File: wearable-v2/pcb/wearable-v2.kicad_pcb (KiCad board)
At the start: 2 copper layers, 78 parts, among them U10 ATmega328PB-M, U11 TMP1075, U12 MAX30102, U13 TCR3UFxxA, U14 LIS2DE12, U2 MCP73832-2-OT, U4 FT201XQ, U9 APDS-9250, Y1 32.768kHz

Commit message: Additional V2 wearable design work
Signed-off-by: Adam Fowler <adam@adamfowler.org>
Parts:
- moved TP16 154.2 mm to (273.6, 19.6)
- moved TP12 148.0 mm to (264.1, 19.8)
- moved TP13 148.0 mm to (264.1, 22.8)
- moved TP14 148.0 mm to (264.1, 25.9)
- moved TP15 148.0 mm to (264.1, 28.9)
- moved U14 142.0 mm to (222.8, 37.1)
- moved C24 121.2 mm to (249.3, 42.1)
- moved C25 120.5 mm to (251.2, 57.4)
- moved C26 120.5 mm to (251.2, 59.4)
- moved TP18 109.5 mm to (229.1, 34.8)
- moved TP17 103.6 mm to (226.8, 42.2)
- moved C21 103.0 mm to (36.4, 24.1)
- moved C17 98.5 mm to (29.6, 29.4)
- moved C18 97.0 mm to (34.3, 28.4)
- moved C28 96.7 mm to (222.3, 46.0)
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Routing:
- net +BATT: track 0.00 -> 25.4 mm
- net /Standard Connector/BT_STAT: track 0.00 -> 23.2 mm
- net GND: track 0.00 -> 21.5 mm, vias 0 -> 5
- net /Bio Board V1/SDA: track 0.00 -> 20.6 mm, vias 0 -> 2
- net /Bio Board V1/SCL: track 0.00 -> 19.7 mm
- net VDD: track 0.00 -> 15.0 mm, vias 0 -> 3
- net VBUS: track 0.00 -> 6.62 mm
- net /Standard Connector/CH_STAT: track 0.00 -> 6.15 mm
- net /Light Sensor Panel V1/LS_INT: track 0.00 -> 4.48 mm
- net Net-(U4-3V3OUT): track 0.00 -> 3.85 mm
- net /Standard Connector/USB_D-: track 0.00 -> 1.99 mm
- net /Standard Connector/USB_D+: track 0.00 -> 1.69 mm
- net Net-(D1-A): track 0.00 -> 1.61 mm
- net Net-(U4-USBDP): track 0.00 -> 1.54 mm
- net Net-(U4-USBDM): track 0.00 -> 1.54 mm
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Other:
- board text added: "ANT"
- board text added: "Bio Board Here"
- board text added: "Compute Board Here"
- board text added: "Deleted???"
- board text added: "Display Board Here"
- board text added: "Front Button Panel"
- board text added: "Front Light Sensor Panel"
- board text added: "GNSS"
- board text added: "Positioning Board Here"
- board text added: "USB-C Here"

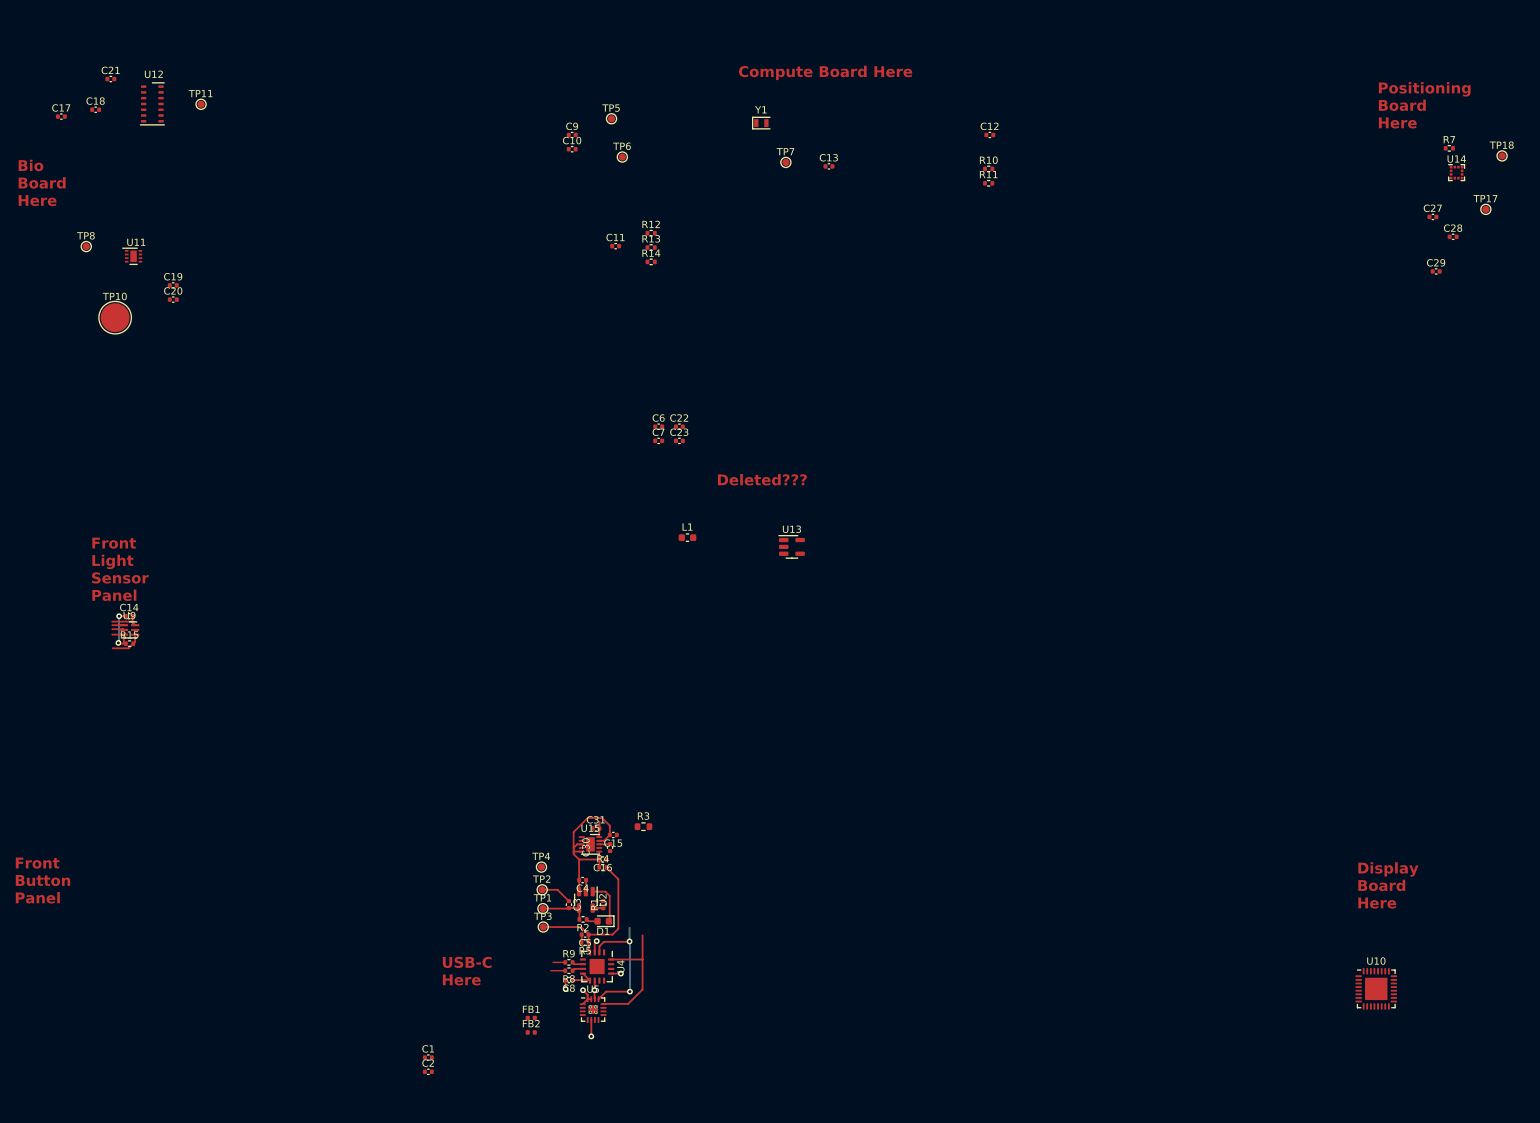
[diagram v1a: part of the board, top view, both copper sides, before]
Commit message: Updated components and PCB layout
Signed-off-by: Adam Fowler <adam@adamfowler.org>
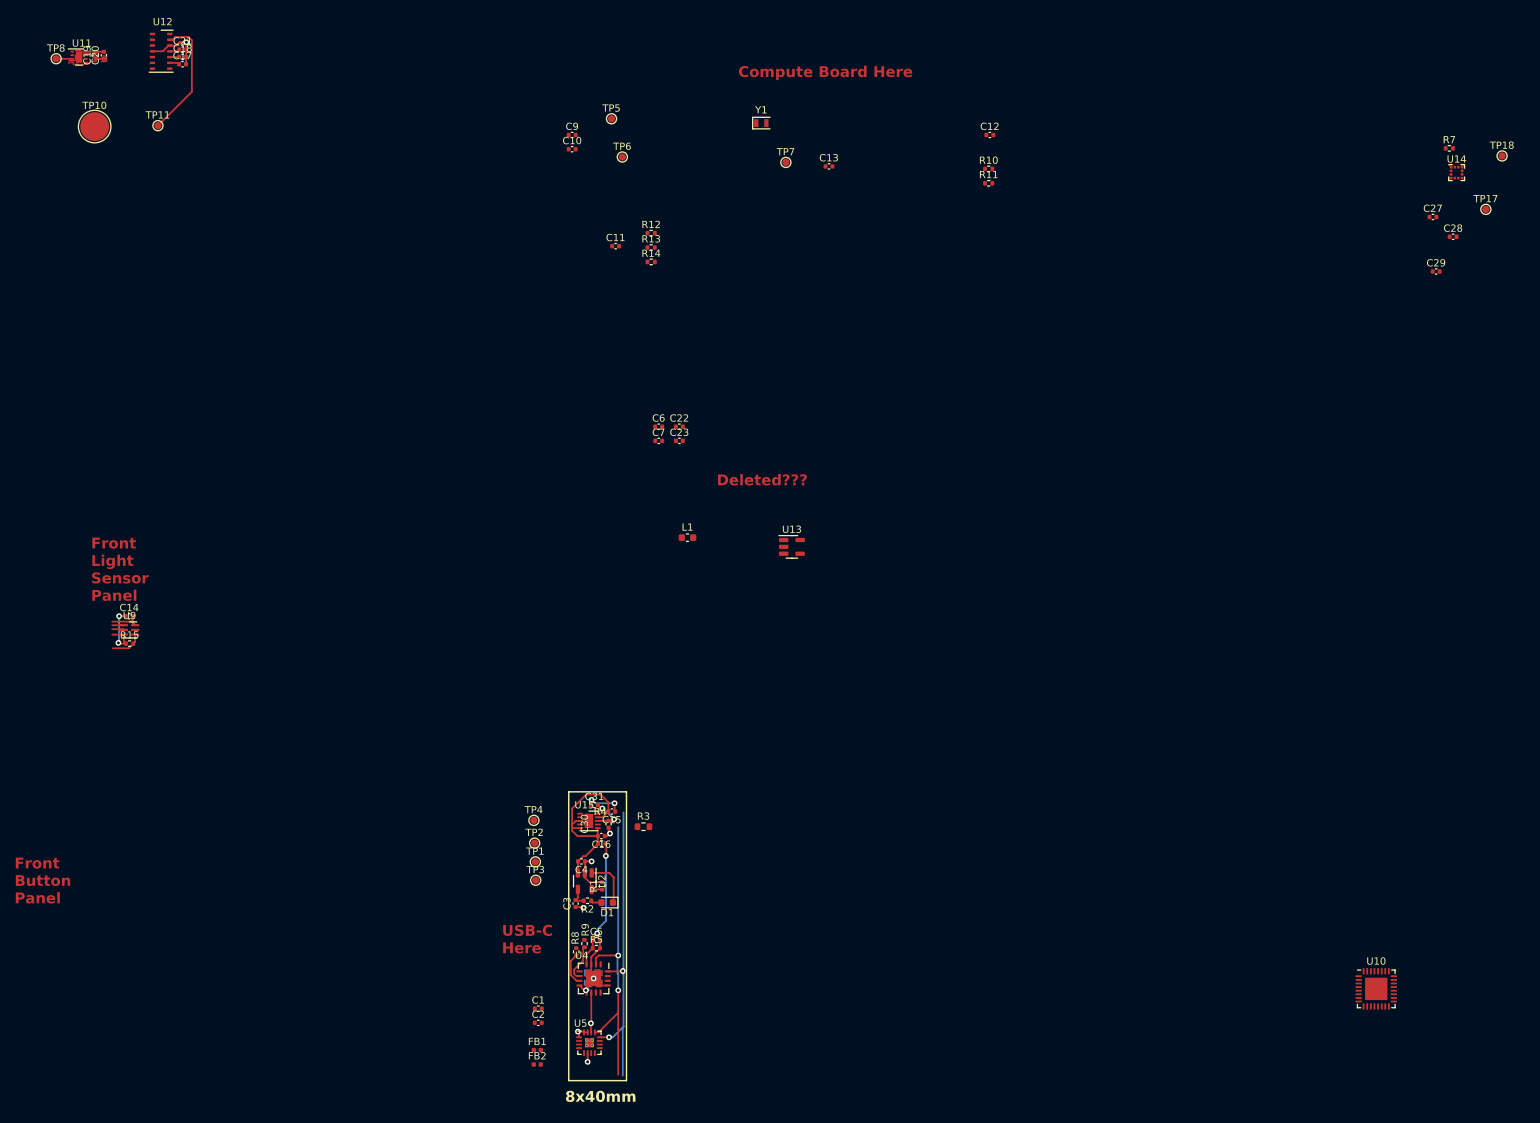
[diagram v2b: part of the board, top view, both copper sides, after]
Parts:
- C8: moved to B.Cu
- moved C20 35.2 mm to (35.4, 20.9), turned to 90 degrees
- moved C19 33.6 mm to (34.3, 20.9), turned to 90 degrees
- moved U11 28.6 mm to (32.0, 21.1)
- moved TP10 26.6 mm to (34.2, 30.7)
- moved TP8 26.3 mm to (28.8, 21.3)
- moved C17 18.3 mm to (46.3, 22.1)
- moved C1 16.7 mm to (95.6, 152.9)
- moved C2 16.7 mm to (95.6, 154.9)
- moved C18 14.1 mm to (46.4, 21.1)
- moved C21 10.8 mm to (46.4, 20.1)
- moved U12 7.39 mm to (43.4, 20.3)
- moved TP11 6.67 mm to (42.9, 30.6)
- moved TP1 6.56 mm to (95.2, 132.6)
- moved TP3 6.56 mm to (95.2, 135.1)
- moved TP4 6.56 mm to (95.0, 126.8)
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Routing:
- net /Bio Board V1/SCL: track 19.7 -> 44.9 mm, vias 0 -> 2
- net /Bio Board V1/SDA: track 20.6 -> 44.8 mm
- net GND: track 21.5 -> 40.1 mm, vias 5 -> 9
- net /Bio Board V1/BIO_INT: track 0.00 -> 17.2 mm
- net VDD: track 15.0 -> 27.3 mm, vias 3 -> 5
- net /Standard Connector/BT_STAT: track 23.2 -> 18.0 mm, vias 0 -> 2
- net VBUS: track 6.62 -> 2.92 mm
- net Net-(U4-USBDP): track 1.54 -> 5.15 mm
- net Net-(U4-USBDM): track 1.54 -> 4.55 mm
- net /Bio Board V1/TMP_INT: track 0.00 -> 2.23 mm
- net /Standard Connector/USB_D-: track 1.99 -> 0.00 mm
- net Net-(U4-3V3OUT): track 3.85 -> 1.98 mm, vias 0 -> 1
- net /Standard Connector/USB_D+: track 1.69 -> 0.00 mm
- net +BATT: track 25.4 -> 26.3 mm
- net /Standard Connector/CH_STAT: track 6.15 -> 6.85 mm
- added copper zone on B.Cu, net GND
- added copper zone on F.Cu, net GND
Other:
- board text added: "35x19mm"
- board text added: "46x46mm"
- board text added: "8x40mm"

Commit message: Further V2 routing
Signed-off-by: Adam Fowler <adam@adamfowler.org>
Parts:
- added ANT1: ~, Herald:NN02-224, F.Cu at (242.1, 59.6)
- added BT1: LiPo, Herald:Herald_Battery_Solder_Pads, F.Cu at (104.8, 117.9)
- added D2: LED_ARBG, Herald:LED_Kingbright_APHF1608, F.Cu at (190.9, 34.3)
- added H1: ThermalSlot, Herald:MillSlot_8.0x1.0mm, F.Cu at (91.4, 81.4)
- added IC1: TESEO-LIV3F, Herald:SON110P970X1010X230-18N, F.Cu at (260.7, 71.7)
- added J7: USB_C_Receptacle_USB2.0, Herald:USB_C_Receptacle_IPxx, F.Cu at (101.1, 142.9)
- added SW1: SW_Push, Button_Switch_SMD:SW_Push_1P1T_NO_CK_KSC6xxJ, F.Cu at (100.6, 172.1)
- added U1: DT1446-04V, Herald:SOT-563, F.Cu at (107.2, 142.9)
- added U3: S-85S1A, Herald:SNT-6A, F.Cu at (114.6, 119.3)
- added U6: BC833, Herald:Fanstel_BC833x, F.Cu at (189.4, 25.6)
- added U7: MX25R8035FZxxx0, Herald:USON-8-1EP_2x3mm_P0.5mm_EP0.25x1.65mm, F.Cu at (184.7, 23.0)
- added U8: PCF85063ATL, Herald:DFN-10-1EP_2.6x2.6mm_P0.5mm_EP1.25x2.15mm, F.Cu at (185.2, 18.3)
- moved C9 86.0 mm to (186.3, 31.1), turned to -90 degrees
- moved R12 83.0 mm to (193.2, 32.3), turned to -90 degrees
- moved R13 82.2 mm to (192.0, 32.3), turned to -90 degrees
- moved R14 81.4 mm to (190.8, 32.3), turned to -90 degrees
- moved TP6 70.8 mm to (178.1, 34.2)
- moved TP5 69.9 mm to (175.5, 34.2)
- moved TP7 63.6 mm to (191.1, 18.5)
- moved Y1 63.1 mm to (188.6, 18.9), turned to 180 degrees
- moved C6 44.6 mm to (115.1, 116.8)
- moved L1 32.3 mm to (118.2, 119.9)
- moved R10 30.0 mm to (185.9, 25.8), turned to 180 degrees
- moved R11 29.2 mm to (182.2, 22.4)
- moved C12 27.2 mm to (182.2, 19.3)
- moved FB2 25.2 mm to (103.6, 136.8), turned to 180 degrees
- moved FB1 22.6 mm to (101.1, 136.8)
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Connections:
- C10 pad 1: VDD -> VDD1
- C11 pad 1: VDD -> VDD1
- C12 pad 2: VDD -> VDD1
- C13 pad 1: VDD -> VDD1
- C14 pad 1: VDD -> +1V8
- C17 pad 1: VDD -> +1V8
- C18 pad 1: VDD -> +1V8
- C19 pad 2: VDD -> +1V8
- C20 pad 2: VDD -> +1V8
- C21 pad 1: VDD -> +1V8
- C23 pad 1: VDD -> +1V8
- C24 pad 1: VDD -> VDD1
- C30 pad 2: VDD -> VDD1
- C31 pad 2: VDD -> +1V8
- R10 pad 1: VDD -> VDD1
- R11 pad 1: VDD -> VDD1
- R15 pad 1: VDD -> +1V8
- TP12 pad 1: VDD -> VDD1
- U10 pad 18: VDD -> VDD1
- U10 pad 4: VDD -> VDD1
- U11 pad 8: VDD -> +1V8
- U12 pad 10: VDD -> +1V8
- U12 pad 11: VDD -> +1V8
- U12 pad 9: VDD -> +1V8
- U13 pad 5: VDD -> +1V8
- U15 pad 10: VDD -> +1V8
- U15 pad 8: VDD -> VDD1
- U9 pad 3: VDD -> +1V8
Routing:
- net /Compute - Fanstel BC833M - Nordic Semi nRF52833 based/SWDCLK: track 0.00 -> 24.5 mm, vias 0 -> 2
- net /Compute - Fanstel BC833M - Nordic Semi nRF52833 based/SWDIO: track 0.00 -> 23.6 mm, vias 0 -> 2
- net VDD: track 27.3 -> 9.15 mm
- net Earth: track 0.00 -> 17.9 mm
- net GNDPWR: track 0.00 -> 15.7 mm
- net +1V8: track 0.00 -> 15.3 mm
- net /Bio Board V1/SDA: track 44.8 -> 58.9 mm
- net /Compute - Fanstel BC833M - Nordic Semi nRF52833 based/LED_B: track 0.00 -> 12.7 mm, vias 0 -> 2
- net VBUS: track 2.92 -> 12.0 mm
- net /Standard Connector/USB_D-: track 0.00 -> 8.76 mm, vias 0 -> 2
- net /Compute - Fanstel BC833M - Nordic Semi nRF52833 based/NFC2: track 0.00 -> 8.72 mm
- net /Compute - Fanstel BC833M - Nordic Semi nRF52833 based/RTC_INT: track 0.00 -> 8.04 mm
- net /Standard Connector/BT_STAT: track 18.0 -> 25.9 mm
- net /Compute - Fanstel BC833M - Nordic Semi nRF52833 based/NFC1: track 0.00 -> 7.51 mm
- net /Compute - Fanstel BC833M - Nordic Semi nRF52833 based/FLASH_CS: track 0.00 -> 7.45 mm
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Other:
- board text removed: "USB-C Here"

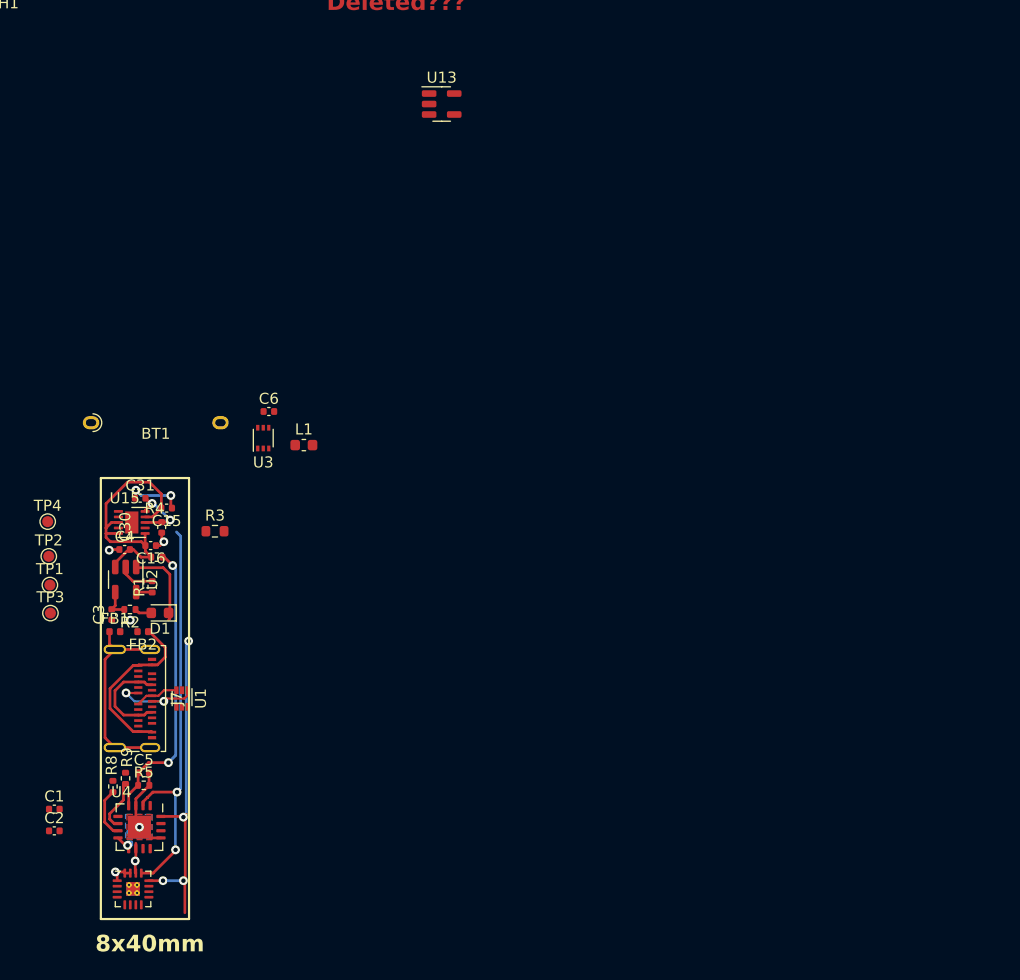
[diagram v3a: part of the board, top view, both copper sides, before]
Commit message: Replaced unavailable I2C chip
Signed-off-by: Adam Fowler <adam@adamfowler.org>
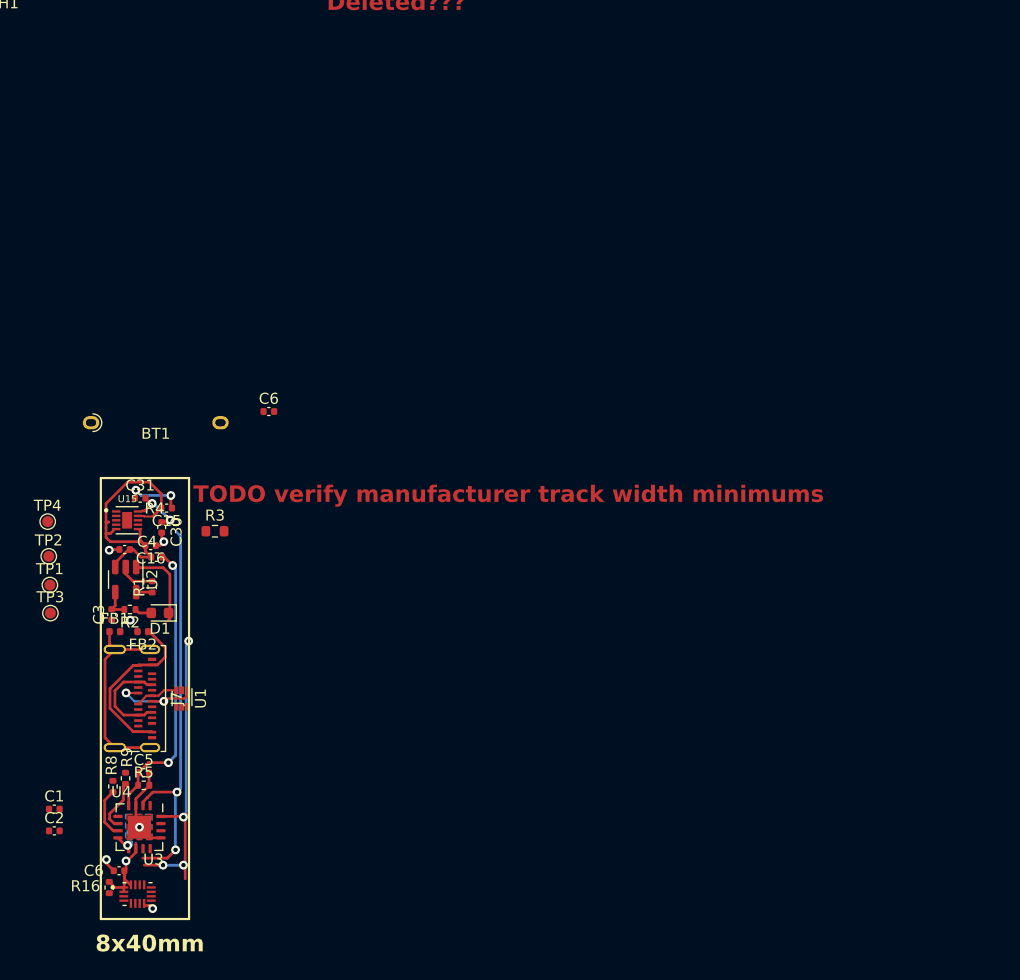
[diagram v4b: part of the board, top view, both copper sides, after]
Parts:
- removed L1: 2.2uH, Inductor_SMD:L_0603_1608Metric
- removed U13: TCR3UFxxA, Package_TO_SOT_SMD:SOT-23-5
- removed U5: ~, Package_DFN_QFN:TQFN-16-1EP_3x3mm_P0.5mm_EP1.23x1.23mm_ThermalVias
- added C6: 4.7uF, Capacitor_SMD:C_0402_1005Metric, F.Cu at (101.5, 158.5)
- added R16: 10k, Resistor_SMD:R_0402_1005Metric, F.Cu at (100.6, 160.0)
- U15: footprint Package_SON:WSON-10-1EP_2.5x2.5mm_P0.5mm_EP1.2x2mm -> Herald:SON40P200X200X80-11N
- U3: value S-85S1A -> TCA6408A; footprint Herald:SNT-6A -> Herald:QFN40P180X260X55-16N
- moved U3 42.9 mm to (103.1, 160.6)
- moved U15 0.47 mm to (102.2, 126.7)
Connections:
- U3 pad 1: VDD -> VDD1
- U3 pad 2: GND -> VDD1
- U3 pad 3: Net-(U3-SW) -> /Standard Connector/RST_CONN
- U3 pad 4: GND -> /Light Sensor Panel V1/LS_INT
- U3 pad 5: +BATT -> /Button Panel V1/BTN_1
- U3 pad 6: +BATT -> /Standard Connector/GPIO_3
- U4 pad 10: VDD -> VDD1
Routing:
- net VDD: track 9.15 -> 0.00 mm
- net VDD1: track 0.00 -> 8.06 mm
- net +1V8: track 15.3 -> 20.4 mm
- net /Bio Board V1/SCL: track 47.6 -> 44.4 mm
- net /Bio Board V1/SDA: track 58.9 -> 58.2 mm
- net GND: track 35.8 -> 35.6 mm, vias 8 -> 9
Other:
- board text added: "TODO verify manufacturer track width minimums"
